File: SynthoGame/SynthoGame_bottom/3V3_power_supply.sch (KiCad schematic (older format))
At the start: 6 parts, among them U2 TLV75533PDBVR, U6 TLV75533PDBVR

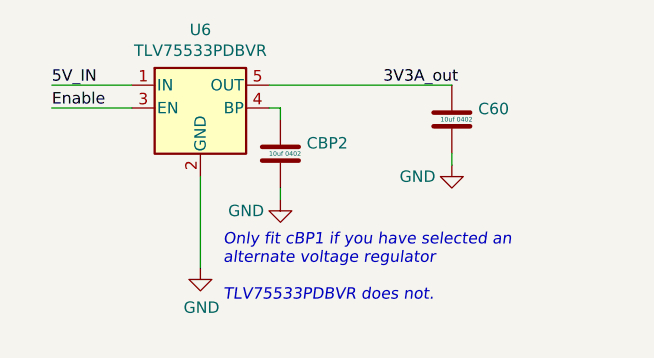
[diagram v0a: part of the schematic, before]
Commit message: connecting I2S - routing
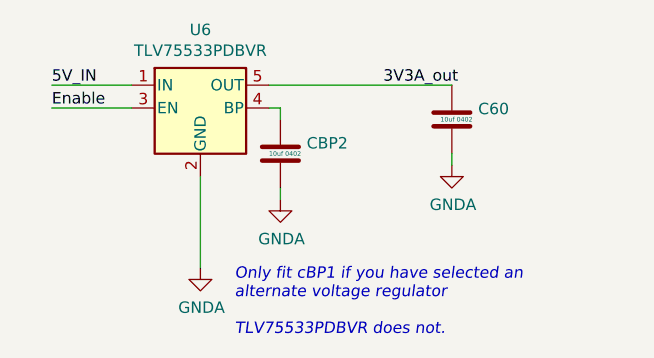
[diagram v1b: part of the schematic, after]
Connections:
- net GND: no longer C60.2, CBP2.2, U6.2 (GND)
- new net GNDA: C60.2, CBP2.2, U6.2 (GND)
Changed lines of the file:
@@
 3V3_out
-$Comp
-L power:GND #PWR?
-U 1 1 6183D2FC
-P 7400 4050
-AR Path="/6183D2FC" Ref="#PWR?"  Part="1"
-AR Path="/617722D3/6183D2FC" Ref="#PWR076"  Part="1"
-F 0 "#PWR076" H 7400 3800 50  0001 C CNN
-F 1 "GND" H 7405 3877 50  0000 C CNN
-F 2 "" H 7400 4050 50  0001 C CNN
-F 3 "" H 7400 4050 50  0001 C CNN
-	1    7400 4050
-	1    0    0    -1
-$EndComp
 $Comp
 L Device:C C?
@@
 F 4 " " H 8500 3400 50  0001 C CNN "LCSC"
 	1    8500 3400
-	1    0    0    -1
-$EndComp
-$Comp
-L power:GND #PWR?
-U 1 1 6183D309
-P 8500 3600
-AR Path="/6183D309" Ref="#PWR?"  Part="1"
-AR Path="/617722D3/6183D309" Ref="#PWR078"  Part="1"
-F 0 "#PWR078" H 8500 3350 50  0001 C CNN
-F 1 "GND" H 8350 3550 50  0000 C CNN
-F 2 "" H 8500 3600 50  0001 C CNN
-F 3 "" H 8500 3600 50  0001 C CNN
-	1    8500 3600
 	1    0    0    -1
 $EndComp
@@
 	1    0    0    -1
 $EndComp
-$Comp
-L power:GND #PWR?
-U 1 1 6183D320
-P 7750 3750
-AR Path="/6183D320" Ref="#PWR?"  Part="1"
-AR Path="/617722D3/6183D320" Ref="#PWR077"  Part="1"
-F 0 "#PWR077" H 7750 3500 50  0001 C CNN
-F 1 "GND" H 7600 3700 50  0000 C CNN
-F 2 "" H 7750 3750 50  0001 C CNN
-F 3 "" H 7750 3750 50  0001 C CNN
-	1    7750 3750
-	1    0    0    -1
-$EndComp
 Wire Wire Line
 	7750 3750 7750 3700
@@
 Wire Wire Line
 	7750 3350 7700 3350
-Text Notes 7500 4200 0    50   Italic 0
+Text Notes 7550 4350 0    50   Italic 0
 Only fit cBP1 if you have selected an \nalternate voltage regulator\n\nTLV75533PDBVR does not.
 Wire Wire Line
@@
 Wire Wire Line
 	3200 3950 3500 3950
+$Comp
+L power:GNDA #PWR?
+U 1 1 61E3B807
+P 7400 4050
+F 0 "#PWR?" H 7400 3800 50  0001 C CNN
+F 1 "GNDA" H 7405 3877 50  0000 C CNN
+F 2 "" H 7400 4050 50  0001 C CNN
+F 3 "" H 7400 4050 50  0001 C CNN
+	1    7400 4050
+	1    0    0    -1
+$EndComp
+$Comp
+L power:GNDA #PWR?
+U 1 1 61E3BBAD
+P 7750 3750
+F 0 "#PWR?" H 7750 3500 50  0001 C CNN
+F 1 "GNDA" H 7755 3577 50  0000 C CNN
+F 2 "" H 7750 3750 50  0001 C CNN
+F 3 "" H 7750 3750 50  0001 C CNN
+	1    7750 3750
+	1    0    0    -1
+$EndComp
+$Comp
+L power:GNDA #PWR?
+U 1 1 61E3BFAB
+P 8500 3600
+F 0 "#PWR?" H 8500 3350 50  0001 C CNN
+F 1 "GNDA" H 8505 3427 50  0000 C CNN
+F 2 "" H 8500 3600 50  0001 C CNN
+F 3 "" H 8500 3600 50  0001 C CNN
+	1    8500 3600
+	1    0    0    -1
+$EndComp
 $EndSCHEMATC

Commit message: resolve ERC errors, minor tweaks
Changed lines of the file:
@@
 $EndComp
-Wire Wire Line
-	5300 3250 6100 3250
 Wire Wire Line
 	5000 3650 5000 4050
@@
 $EndComp
 Wire Wire Line
-	7700 3250 8500 3250
-Wire Wire Line
-	7400 3650 7400 4050
+	7400 3650 7400 4000
 $Comp
 L Device:C CBP?
@@
 	1    0    0    -1
 $EndComp
+Wire Wire Line
+	7700 3250 8500 3250
+$Comp
+L power:PWR_FLAG #FLG0103
+U 1 1 61958885
+P 7100 3975
+F 0 "#FLG0103" H 7100 4050 50  0001 C CNN
+F 1 "PWR_FLAG" H 7100 4148 50  0000 C CNN
+F 2 "" H 7100 3975 50  0001 C CNN
+F 3 "~" H 7100 3975 50  0001 C CNN
+	1    7100 3975
+	1    0    0    -1
+$EndComp
+Wire Wire Line
+	7100 3975 7100 4000
+Wire Wire Line
+	7100 4000 7400 4000
+Wire Wire Line
+	5300 3250 6100 3250
+Connection ~ 7400 4000
+Wire Wire Line
+	7400 4000 7400 4050
 $EndSCHEMATC
